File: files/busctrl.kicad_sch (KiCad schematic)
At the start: 5 parts, among them J1 VLB_slot, U10 74LS245, U2 27C020

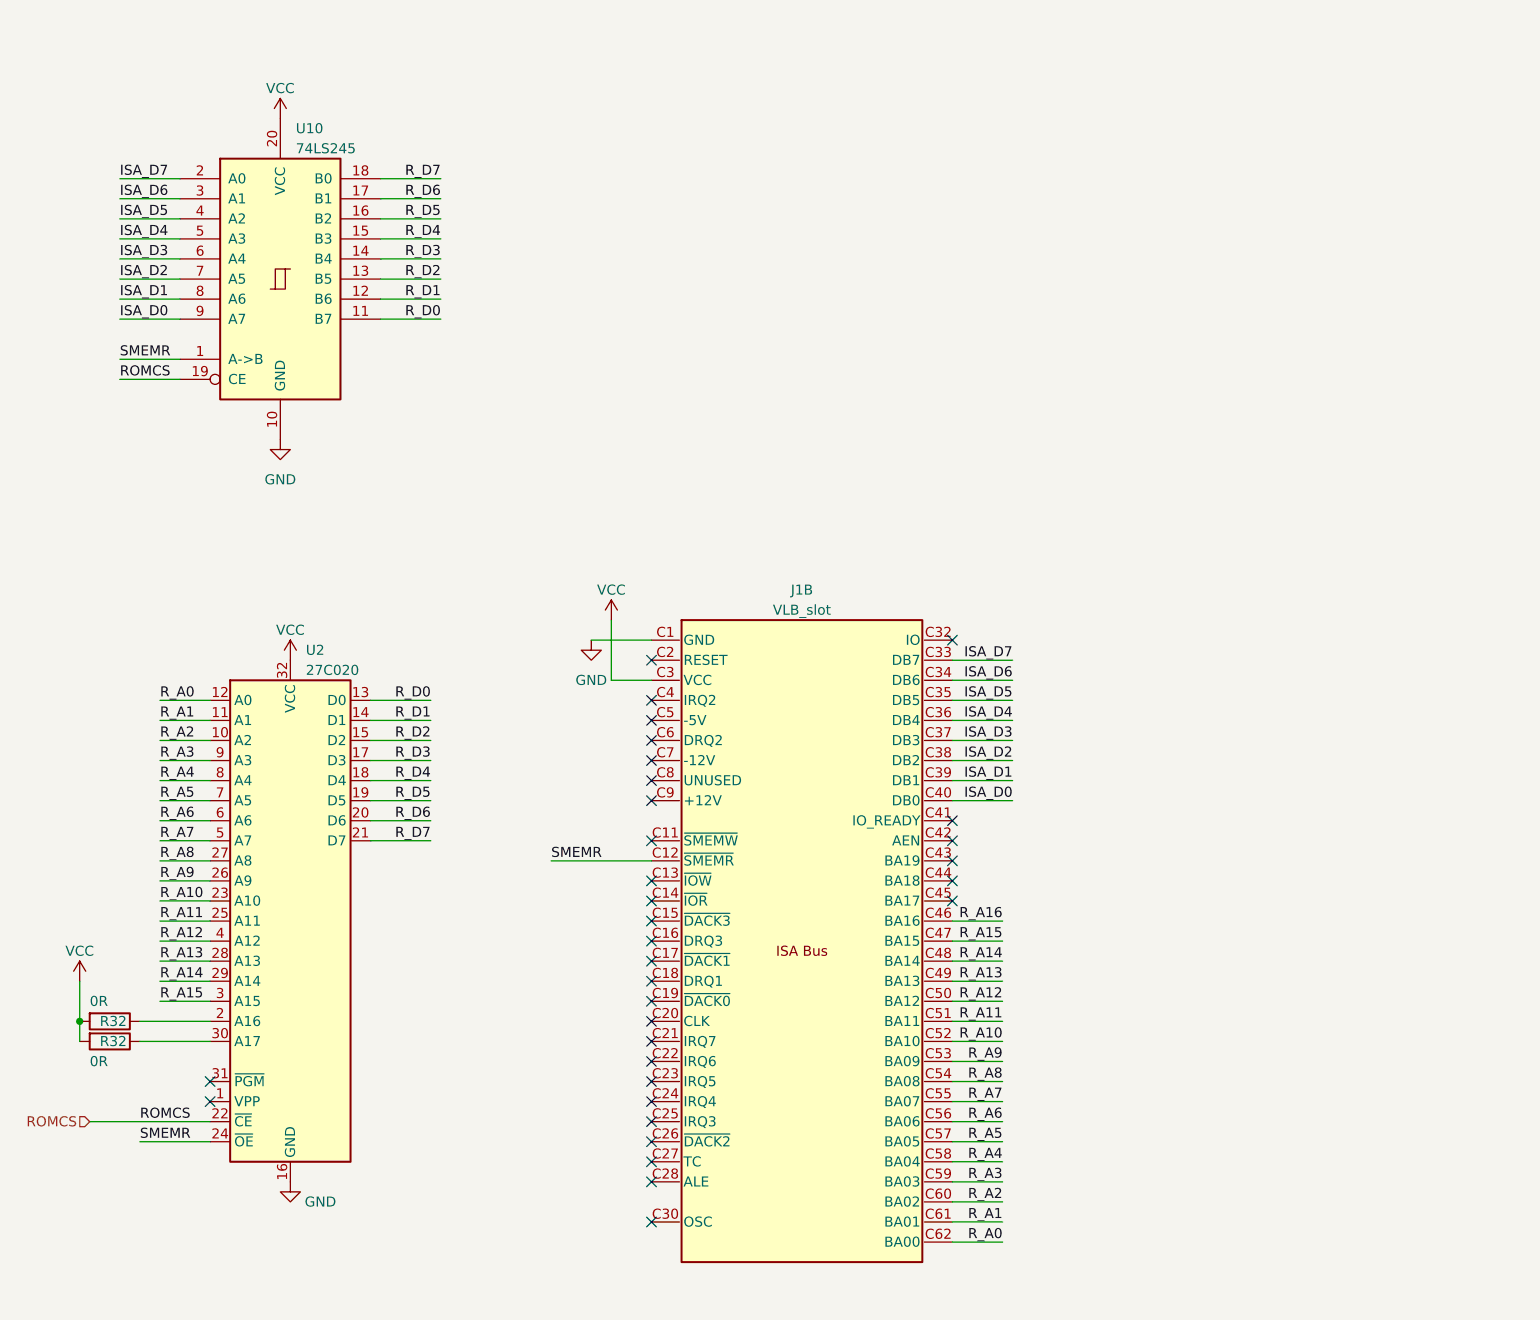
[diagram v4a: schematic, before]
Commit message: added SAUP decoding, adjusted VGA conn.
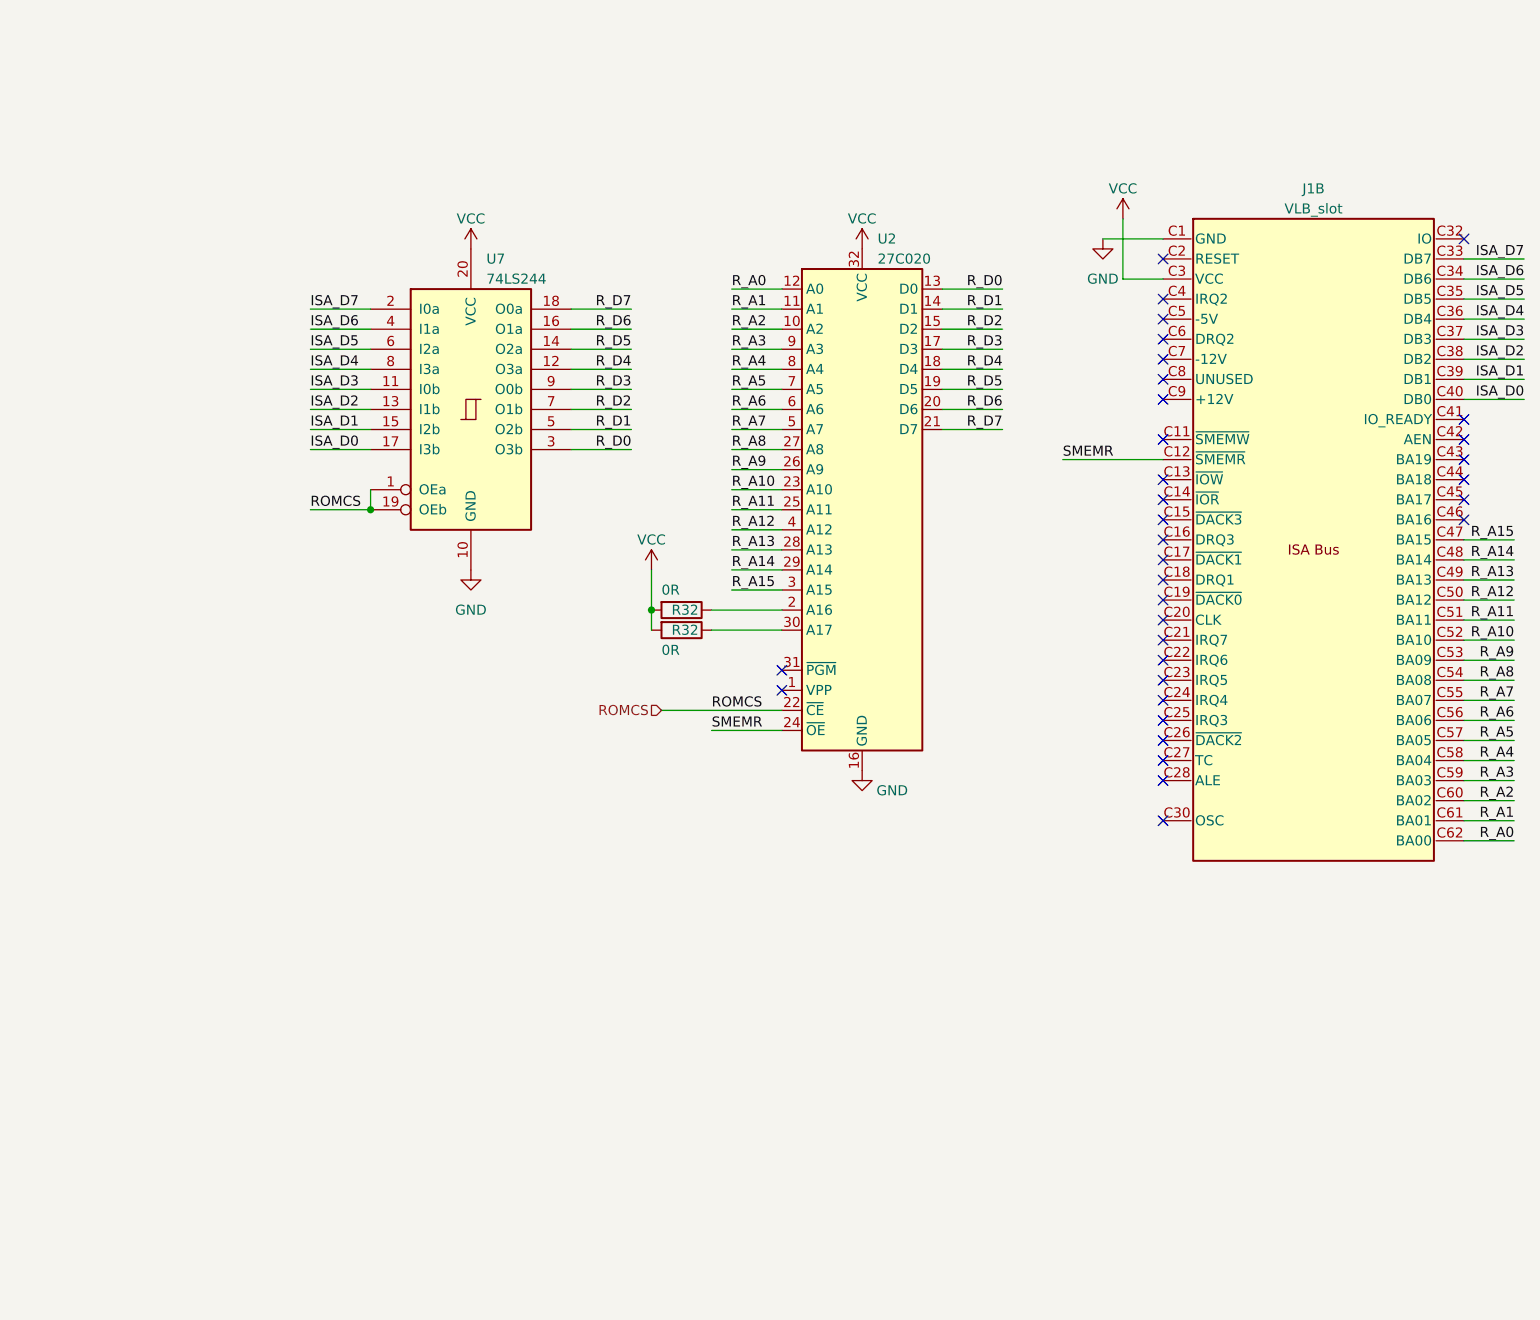
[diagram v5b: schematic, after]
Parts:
- removed U10: 74LS245, Package_SO:SO-20_5.3x12.6mm_P1.27mm, symbol 74xx:74LS245
- added U7: 74LS244, Package_SO:SO-20_5.3x12.6mm_P1.27mm, symbol 74xx:74LS244
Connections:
- net GND: now also U7.10 (GND)
- net ISA_D0: now also U7.17 (I3b)
- net ISA_D1: now also U7.15 (I2b)
- net ISA_D2: now also U7.13 (I1b)
- net ISA_D3: now also U7.11 (I0b)
- net ISA_D4: now also U7.8 (I3a)
- net ISA_D5: now also U7.6 (I2a)
- net ISA_D6: now also U7.4 (I1a)
- net ISA_D7: now also U7.2 (I0a)
- net ROMCS: now also U7.1 (OEa), U7.19 (OEb)
- net R_D0: now also U7.3 (O3b)
- net R_D1: now also U7.5 (O2b)
- net R_D2: now also U7.7 (O1b)
- net R_D3: now also U7.9 (O0b)
- net R_D4: now also U7.12 (O3a)
- net R_D5: now also U7.14 (O2a)
- net R_D6: now also U7.16 (O1a)
- net R_D7: now also U7.18 (O0a)
- net VCC: now also U7.20 (VCC)
- net R_A16: no longer names the net of J1.C46 (BA16)
- no-connect marks 33 -> 34
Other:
- moved on the sheet: J1B, R32, U2

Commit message: Board review changes 2023-07-06
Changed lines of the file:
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@@
     (stroke (width 0) (type default))
   )
-  (wire (pts (xy 201.93 127) (xy 195.58 127))
+  (wire (pts (xy 195.58 127) (xy 203.2 127))
     (stroke (width 0) (type default))
   )
@@
     (stroke (width 0) (type default))
   )
+  (wire (pts (xy 195.58 111.76) (xy 203.2 111.76))
+    (stroke (width 0) (type default))
+  )
+  (wire (pts (xy 195.58 104.14) (xy 203.2 104.14))
+    (stroke (width 0) (type default))
+  )
   (wire (pts (xy 102.87 67.31) (xy 109.22 67.31))
     (stroke (width 0) (type default))
@@
     (stroke (width 0) (type default))
   )
-  (wire (pts (xy 201.93 124.46) (xy 195.58 124.46))
-    (stroke (width 0) (type default))
-  )
   (wire (pts (xy 157.48 66.04) (xy 152.4 66.04))
     (stroke (width 0) (type default))
@@
     (stroke (width 0) (type default))
   )
-  (wire (pts (xy 201.93 106.68) (xy 195.58 106.68))
-    (stroke (width 0) (type default))
-  )
   (wire (pts (xy 102.87 102.87) (xy 109.22 102.87))
     (stroke (width 0) (type default))
@@
     (stroke (width 0) (type default))
   )
-  (wire (pts (xy 201.93 134.62) (xy 195.58 134.62))
-    (stroke (width 0) (type default))
-  )
-  (wire (pts (xy 201.93 114.3) (xy 195.58 114.3))
+  (wire (pts (xy 195.58 114.3) (xy 203.2 114.3))
+    (stroke (width 0) (type default))
+  )
+  (wire (pts (xy 195.58 99.06) (xy 203.2 99.06))
     (stroke (width 0) (type default))
   )
@@
     (stroke (width 0) (type default))
   )
+  (wire (pts (xy 195.58 116.84) (xy 203.2 116.84))
+    (stroke (width 0) (type default))
+  )
   (wire (pts (xy 129.54 77.47) (xy 137.16 77.47))
     (stroke (width 0) (type default))
@@
     (stroke (width 0) (type default))
   )
-  (wire (pts (xy 201.93 132.08) (xy 195.58 132.08))
-    (stroke (width 0) (type default))
-  )
-  (wire (pts (xy 201.93 129.54) (xy 195.58 129.54))
+  (wire (pts (xy 195.58 101.6) (xy 203.2 101.6))
+    (stroke (width 0) (type default))
+  )
+  (wire (pts (xy 195.58 132.08) (xy 203.2 132.08))
     (stroke (width 0) (type default))
   )
@@
     (stroke (width 0) (type default))
   )
-  (wire (pts (xy 201.93 104.14) (xy 195.58 104.14))
-    (stroke (width 0) (type default))
-  )
-  (wire (pts (xy 201.93 119.38) (xy 195.58 119.38))
+  (wire (pts (xy 195.58 134.62) (xy 203.2 134.62))
+    (stroke (width 0) (type default))
+  )
+  (wire (pts (xy 195.58 124.46) (xy 203.2 124.46))
+    (stroke (width 0) (type default))
+  )
+  (wire (pts (xy 195.58 119.38) (xy 203.2 119.38))
     (stroke (width 0) (type default))
   )
@@
     (stroke (width 0) (type default))
   )
-  (wire (pts (xy 201.93 101.6) (xy 195.58 101.6))
-    (stroke (width 0) (type default))
-  )
   (wire (pts (xy 195.58 78.74) (xy 203.2 78.74))
     (stroke (width 0) (type default))
@@
     (stroke (width 0) (type default))
   )
-  (wire (pts (xy 201.93 137.16) (xy 195.58 137.16))
+  (wire (pts (xy 195.58 137.16) (xy 203.2 137.16))
     (stroke (width 0) (type default))
   )
@@
     (stroke (width 0) (type default))
   )
-  (wire (pts (xy 201.93 116.84) (xy 195.58 116.84))
-    (stroke (width 0) (type default))
-  )
   (wire (pts (xy 102.87 92.71) (xy 109.22 92.71))
     (stroke (width 0) (type default))
@@
     (stroke (width 0) (type default))
   )
-  (wire (pts (xy 201.93 109.22) (xy 195.58 109.22))
+  (wire (pts (xy 195.58 109.22) (xy 203.2 109.22))
     (stroke (width 0) (type default))
   )
@@
     (stroke (width 0) (type default))
   )
+  (wire (pts (xy 195.58 106.68) (xy 203.2 106.68))
+    (stroke (width 0) (type default))
+  )
   (wire (pts (xy 129.54 82.55) (xy 137.16 82.55))
     (stroke (width 0) (type default))
@@
     (stroke (width 0) (type default))
   )
-  (wire (pts (xy 201.93 99.06) (xy 195.58 99.06))
-    (stroke (width 0) (type default))
-  )
-  (wire (pts (xy 201.93 111.76) (xy 195.58 111.76))
-    (stroke (width 0) (type default))
-  )
   (wire (pts (xy 57.15 92.71) (xy 57.15 95.25))
     (stroke (width 0) (type default))
@@
     (stroke (width 0) (type default))
   )
+  (wire (pts (xy 195.58 129.54) (xy 203.2 129.54))
+    (stroke (width 0) (type default))
+  )
   (wire (pts (xy 149.86 60.96) (xy 157.48 60.96))
     (stroke (width 0) (type default))
   )
-  (wire (pts (xy 201.93 121.92) (xy 195.58 121.92))
+  (wire (pts (xy 195.58 121.92) (xy 203.2 121.92))
     (stroke (width 0) (type default))
   )
@@
     (effects (font (size 1.27 1.27)) (justify left bottom))
   )
-  (label "R_A1" (at 201.93 134.62 180) (fields_autoplaced)
-    (effects (font (size 1.27 1.27)) (justify right bottom))
-  )
-  (label "R_A3" (at 201.93 129.54 180) (fields_autoplaced)
+  (label "R_A1" (at 203.2 134.62 180) (fields_autoplaced)
+    (effects (font (size 1.27 1.27)) (justify right bottom))
+  )
+  (label "R_A3" (at 203.2 129.54 180) (fields_autoplaced)
     (effects (font (size 1.27 1.27)) (justify right bottom))
   )
@@
     (effects (font (size 1.27 1.27)) (justify left bottom))
   )
-  (label "R_A15" (at 201.93 99.06 180) (fields_autoplaced)
+  (label "R_A15" (at 203.2 99.06 180) (fields_autoplaced)
     (effects (font (size 1.27 1.27)) (justify right bottom))
   )
@@
     (effects (font (size 1.27 1.27)) (justify left bottom))
   )
-  (label "R_A13" (at 201.93 104.14 180) (fields_autoplaced)
-    (effects (font (size 1.27 1.27)) (justify right bottom))
-  )
-  (label "R_A12" (at 201.93 106.68 180) (fields_autoplaced)
-    (effects (font (size 1.27 1.27)) (justify right bottom))
-  )
-  (label "R_A4" (at 201.93 127 180) (fields_autoplaced)
+  (label "R_A13" (at 203.2 104.14 180) (fields_autoplaced)
+    (effects (font (size 1.27 1.27)) (justify right bottom))
+  )
+  (label "R_A12" (at 203.2 106.68 180) (fields_autoplaced)
+    (effects (font (size 1.27 1.27)) (justify right bottom))
+  )
+  (label "R_A4" (at 203.2 127 180) (fields_autoplaced)
     (effects (font (size 1.27 1.27)) (justify right bottom))
   )
@@
     (effects (font (size 1.27 1.27)) (justify left bottom))
   )
-  (label "R_A11" (at 201.93 109.22 180) (fields_autoplaced)
-    (effects (font (size 1.27 1.27)) (justify right bottom))
-  )
-  (label "R_A7" (at 201.93 119.38 180) (fields_autoplaced)
+  (label "R_A11" (at 203.2 109.22 180) (fields_autoplaced)
+    (effects (font (size 1.27 1.27)) (justify right bottom))
+  )
+  (label "R_A7" (at 203.2 119.38 180) (fields_autoplaced)
     (effects (font (size 1.27 1.27)) (justify right bottom))
   )
@@
     (effects (font (size 1.27 1.27)) (justify left bottom))
   )
-  (label "R_A9" (at 201.93 114.3 180) (fields_autoplaced)
-    (effects (font (size 1.27 1.27)) (justify right bottom))
-  )
-  (label "R_A0" (at 201.93 137.16 180) (fields_autoplaced)
+  (label "R_A9" (at 203.2 114.3 180) (fields_autoplaced)
+    (effects (font (size 1.27 1.27)) (justify right bottom))
+  )
+  (label "R_A0" (at 203.2 137.16 180) (fields_autoplaced)
     (effects (font (size 1.27 1.27)) (justify right bottom))
   )
@@
     (effects (font (size 1.27 1.27)) (justify left bottom))
   )
-  (label "R_A10" (at 201.93 111.76 180) (fields_autoplaced)
+  (label "R_A10" (at 203.2 111.76 180) (fields_autoplaced)
     (effects (font (size 1.27 1.27)) (justify right bottom))
   )
@@
     (effects (font (size 1.27 1.27)) (justify right bottom))
   )
-  (label "R_A14" (at 201.93 101.6 180) (fields_autoplaced)
+  (label "R_A14" (at 203.2 101.6 180) (fields_autoplaced)
     (effects (font (size 1.27 1.27)) (justify right bottom))
   )
@@
     (effects (font (size 1.27 1.27)) (justify left bottom))
   )
-  (label "R_A8" (at 201.93 116.84 180) (fields_autoplaced)
+  (label "R_A8" (at 203.2 116.84 180) (fields_autoplaced)
     (effects (font (size 1.27 1.27)) (justify right bottom))
   )
@@
     (effects (font (size 1.27 1.27)) (justify right bottom))
   )
-  (label "R_A2" (at 201.93 132.08 180) (fields_autoplaced)
+  (label "R_A2" (at 203.2 132.08 180) (fields_autoplaced)
     (effects (font (size 1.27 1.27)) (justify right bottom))
   )
@@
     (effects (font (size 1.27 1.27)) (justify left bottom))
   )
-  (label "R_A5" (at 201.93 124.46 180) (fields_autoplaced)
+  (label "R_A5" (at 203.2 124.46 180) (fields_autoplaced)
     (effects (font (size 1.27 1.27)) (justify right bottom))
   )
@@
     (effects (font (size 1.27 1.27)) (justify left bottom))
   )
-  (label "R_A6" (at 201.93 121.92 180) (fields_autoplaced)
-    (effects (font (size 1.27 1.27)) (justify right bottom))
-  )
-  (hierarchical_label "ROMCS" (shape input) (at 93.98 120.65 180) (fields_autoplaced)
+  (label "R_A6" (at 203.2 121.92 180) (fields_autoplaced)
+    (effects (font (size 1.27 1.27)) (justify right bottom))
+  )
+  (global_label "ROMCS" (shape input) (at 93.98 120.65 180) (fields_autoplaced)
     (effects (font (size 1.27 1.27)) (justify right))
+    (property "Intersheetrefs" "${INTERSHEET_REFS}" (at 84.5428 120.65 0)
+      (effects (font (size 1.27 1.27)) (justify right) hide)
+    )
   )
   (symbol (lib_id "power:GND") (at 149.86 60.96 0) (unit 1)
